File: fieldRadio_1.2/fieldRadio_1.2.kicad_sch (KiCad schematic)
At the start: 11 parts, among them J1 Conn_01x02, J12 AudioJack3_Switch, J18 Conn_01x16, J2 Conn_01x02, J3 Conn_01x03, J4 AudioJack2_Switch, J5 AudioJack3_Switch, J7 Conn_01x04, J8 Conn_01x12

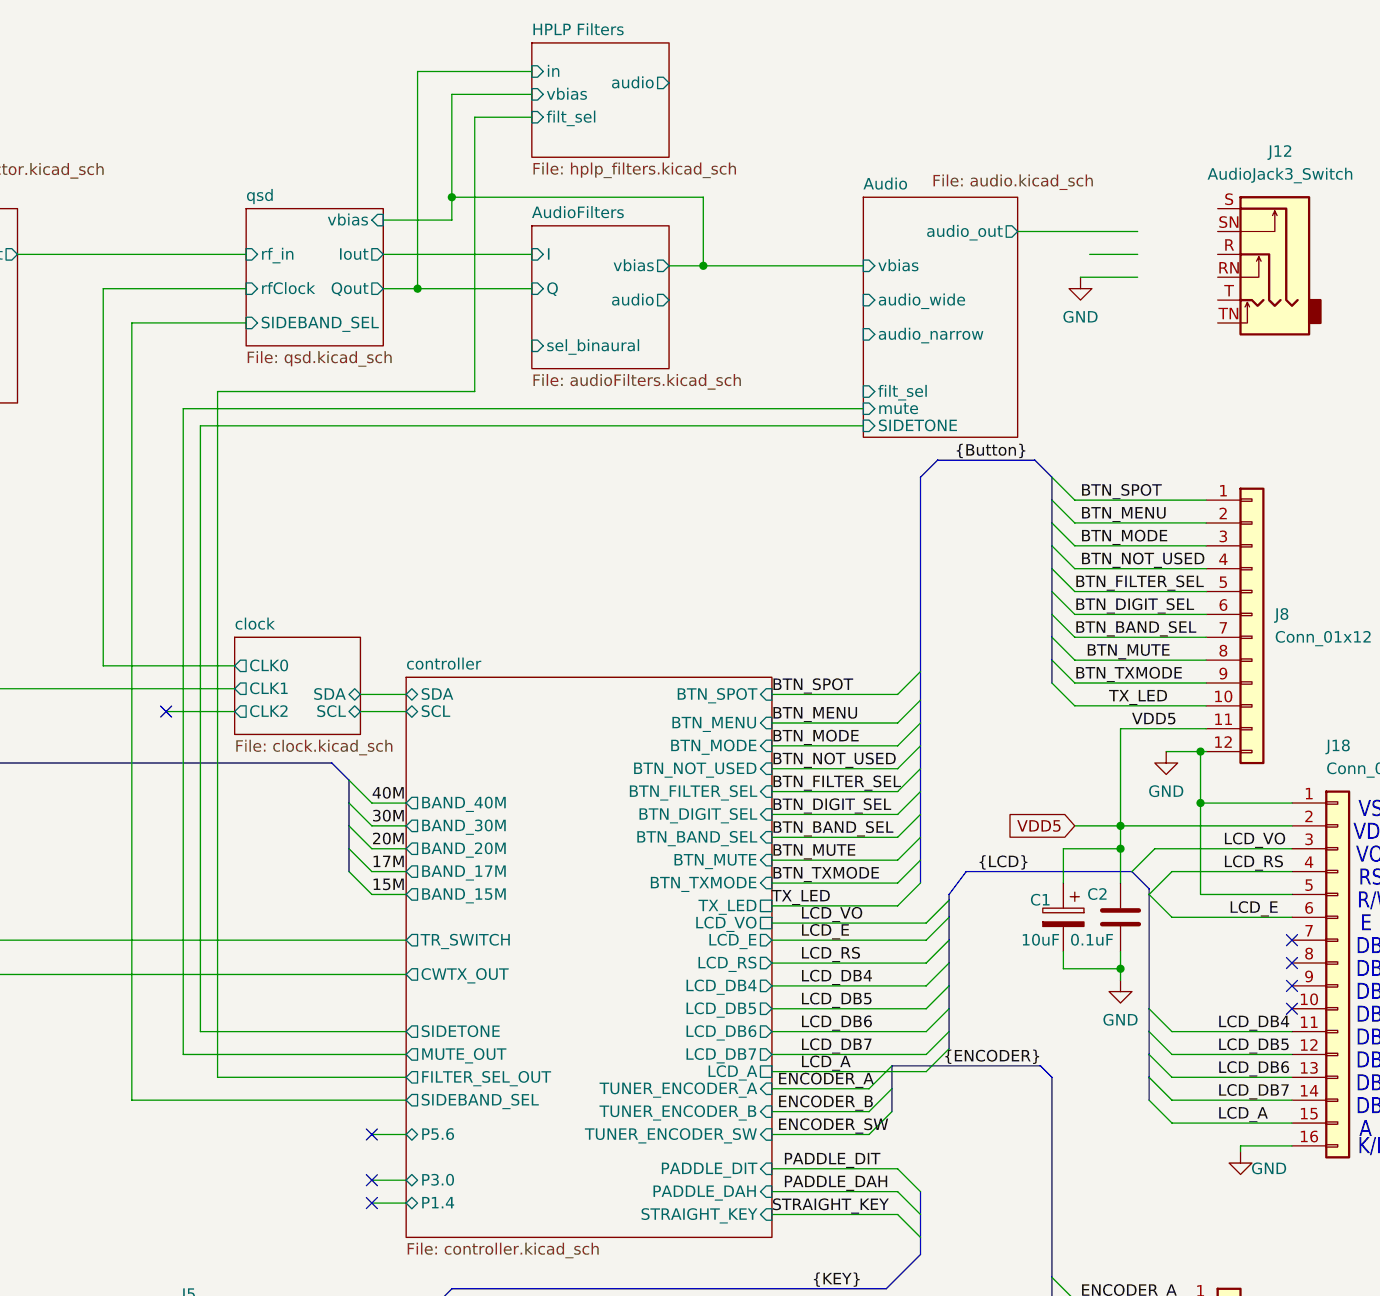
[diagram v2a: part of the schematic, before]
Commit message: Finished first pass of audio schematic changes for binaural/mono
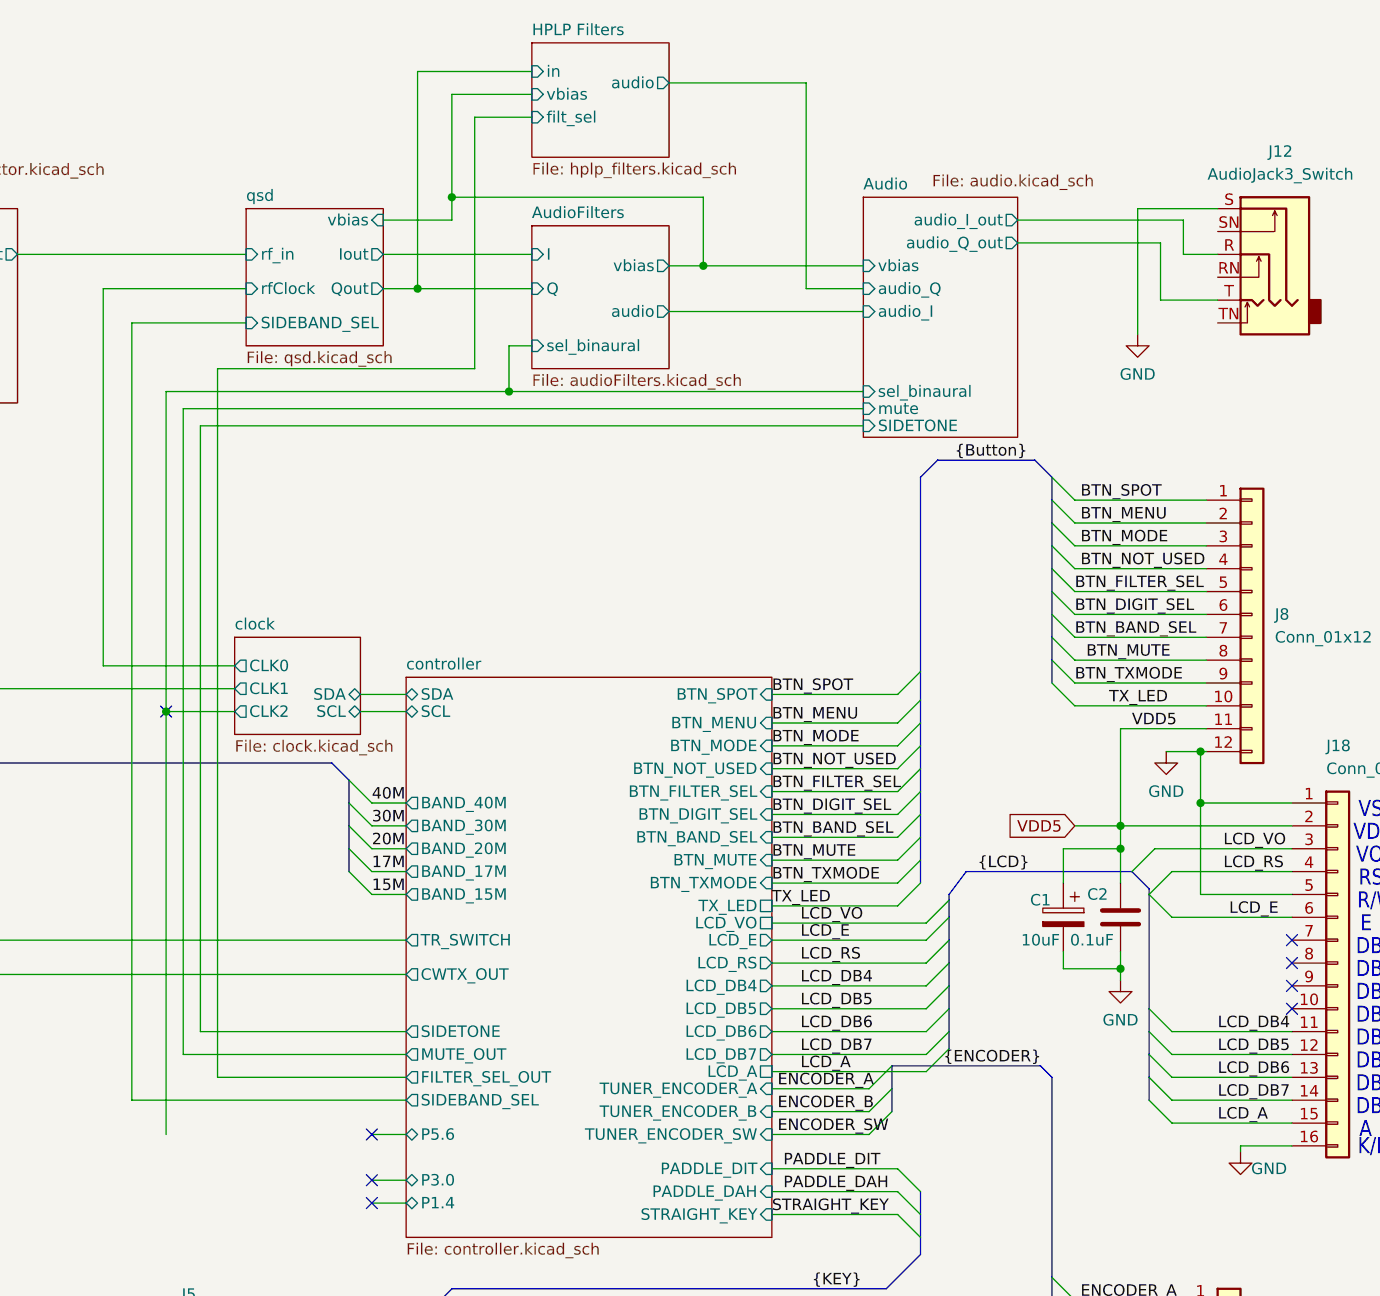
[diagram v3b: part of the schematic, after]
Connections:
- net GND: now also J12.S
- net Audio/audio_I_out: now reaches J12.R
- net Audio/audio_Q_out: now reaches J12.T
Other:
- sheet Audio ports: added audio_I, audio_I_out, audio_Q, audio_Q_out, sel_binaural; removed audio_narrow, audio_out, audio_wide, filt_sel
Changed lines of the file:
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@@
 	)
 	(junction
+		(at 144.78 90.17)
+		(diameter 0)
+		(color 0 0 0 0)
+	)
+	(junction
 		(at 204.47 40.64)
 		(diameter 0)
@@
 	)
 	(junction
+		(at 182.88 54.61)
+		(diameter 0)
+		(color 0 0 0 0)
+	)
+	(junction
 		(at 250.825 105.41)
 		(diameter 0)
@@
 		)
 	)
+	(wire
+		(pts
+			(xy 252.73 34.29) (xy 252.73 48.26)
+		)
+		(stroke
+			(width 0)
+			(type default)
+		)
+	)
 	(bus
 		(pts
@@
 	(wire
 		(pts
-			(xy 150.495 130.81) (xy 150.495 54.61)
+			(xy 150.495 130.81) (xy 150.495 52.07)
 		)
 		(stroke
@@
 	(wire
 		(pts
+			(xy 144.78 90.17) (xy 144.78 137.16)
+		)
+		(stroke
+			(width 0)
+			(type default)
+		)
+	)
+	(wire
+		(pts
 			(xy 171.45 130.81) (xy 150.495 130.81)
 		)
@@
 	(wire
 		(pts
+			(xy 182.88 49.53) (xy 182.88 54.61)
+		)
+		(stroke
+			(width 0)
+			(type default)
+		)
+	)
+	(wire
+		(pts
 			(xy 146.685 56.515) (xy 222.25 56.515)
 		)
@@
 	(wire
 		(pts
+			(xy 255.27 44.45) (xy 261.62 44.45)
+		)
+		(stroke
+			(width 0)
+			(type default)
+		)
+	)
+	(wire
+		(pts
 			(xy 250.825 102.87) (xy 269.875 102.87)
 		)
@@
 	(wire
 		(pts
+			(xy 257.81 35.56) (xy 257.81 39.37)
+		)
+		(stroke
+			(width 0)
+			(type default)
+		)
+	)
+	(wire
+		(pts
 			(xy 259.715 110.49) (xy 269.875 110.49)
 		)
@@
 	(wire
 		(pts
+			(xy 222.25 54.61) (xy 182.88 54.61)
+		)
+		(stroke
+			(width 0)
+			(type default)
+		)
+	)
+	(wire
+		(pts
+			(xy 239.395 35.56) (xy 257.81 35.56)
+		)
+		(stroke
+			(width 0)
+			(type default)
+		)
+	)
+	(wire
+		(pts
 			(xy 71.755 180.34) (xy 71.755 184.785)
 		)
@@
 	(wire
 		(pts
-			(xy 150.495 54.61) (xy 179.07 54.61)
+			(xy 150.495 52.07) (xy 179.07 52.07)
 		)
 		(stroke
@@
 	(wire
 		(pts
+			(xy 215.9 43.18) (xy 222.25 43.18)
+		)
+		(stroke
+			(width 0)
+			(type default)
+		)
+	)
+	(wire
+		(pts
 			(xy 212.09 134.62) (xy 222.885 134.62)
 		)
@@
 	(wire
 		(pts
-			(xy 252.73 39.37) (xy 247.396 39.37)
-		)
-		(stroke
-			(width 0)
-			(type default)
-		)
-	)
-	(wire
-		(pts
 			(xy 256.54 128.27) (xy 269.875 128.27)
 		)
@@
 		)
 	)
+	(wire
+		(pts
+			(xy 257.81 39.37) (xy 261.62 39.37)
+		)
+		(stroke
+			(width 0)
+			(type default)
+		)
+	)
 	(bus
 		(pts
@@
 		)
 	)
-	(wire
+	(bus
 		(pts
-			(xy 246.38 41.91) (xy 252.73 41.91)
+			(xy 228.6 148.59) (xy 228.6 150.495)
 		)
 		(stroke
@@
 	(bus
 		(pts
-			(xy 228.6 148.59) (xy 228.6 150.495)
+			(xy 165.1 97.79) (xy 165.1 100.33)
 		)
 		(stroke
@@
 		)
 	)
-	(bus
+	(wire
 		(pts
-			(xy 165.1 97.79) (xy 165.1 100.33)
+			(xy 144.78 54.61) (xy 144.78 90.17)
 		)
 		(stroke
@@
 		)
 	)
+	(wire
+		(pts
+			(xy 215.9 20.32) (xy 215.9 43.18)
+		)
+		(stroke
+			(width 0)
+			(type default)
+		)
+	)
 	(bus
 		(pts
@@
 	(wire
 		(pts
+			(xy 239.395 38.1) (xy 255.27 38.1)
+		)
+		(stroke
+			(width 0)
+			(type default)
+		)
+	)
+	(wire
+		(pts
 			(xy 31.496 175.26) (xy 41.91 175.26)
 		)
@@
 		)
 	)
+	(wire
+		(pts
+			(xy 255.27 38.1) (xy 255.27 44.45)
+		)
+		(stroke
+			(width 0)
+			(type default)
+		)
+	)
 	(bus
 		(pts
@@
 	(wire
 		(pts
-			(xy 179.07 24.13) (xy 179.07 54.61)
+			(xy 179.07 24.13) (xy 179.07 52.07)
 		)
 		(stroke
@@
 	(wire
 		(pts
+			(xy 182.88 54.61) (xy 144.78 54.61)
+		)
+		(stroke
+			(width 0)
+			(type default)
+		)
+	)
+	(wire
+		(pts
 			(xy 200.66 40.64) (xy 204.47 40.64)
 		)
@@
 		)
 	)
+	(wire
+		(pts
+			(xy 200.66 20.32) (xy 215.9 20.32)
+		)
+		(stroke
+			(width 0)
+			(type default)
+		)
+	)
 	(bus
 		(pts
@@
 		)
 	)
+	(wire
+		(pts
+			(xy 200.66 45.72) (xy 222.25 45.72)
+		)
+		(stroke
+			(width 0)
+			(type default)
+		)
+	)
 	(bus
 		(pts
@@
 	(wire
 		(pts
-			(xy 239.395 36.83) (xy 252.73 36.83)
-		)
-		(stroke
-			(width 0)
-			(type default)
-		)
-	)
-	(wire
-		(pts
 			(xy 167.64 137.16) (xy 171.45 137.16)
 		)
@@
 	(wire
 		(pts
+			(xy 185.42 49.53) (xy 182.88 49.53)
+		)
+		(stroke
+			(width 0)
+			(type default)
+		)
+	)
+	(wire
+		(pts
 			(xy 167.64 100.33) (xy 171.45 100.33)
 		)
@@
 	(wire
 		(pts
+			(xy 261.62 34.29) (xy 252.73 34.29)
+		)
+		(stroke
+			(width 0)
+			(type default)
+		)
+	)
+	(wire
+		(pts
 			(xy 56.515 43.18) (xy 64.77 43.18)
 		)
@@
 	(symbol
 		(lib_id "power:GND")
-		(at 246.38 41.91 0)
+		(at 252.73 48.26 0)
 		(unit 1)
 		(exclude_from_sim no)
@@
 		(fields_autoplaced yes)
 		(property "Reference" "#PWR04"
-			(at 246.38 48.26 0)
+			(at 252.73 54.61 0)
 			(effects
 				(font
@@
 		)
 		(property "Value" "GND"
-			(at 246.38 46.355 0)
+			(at 252.73 52.705 0)
 			(effects
 				(font
@@
 		)
 		(property "Footprint" ""
-			(at 246.38 41.91 0)
+			(at 252.73 48.26 0)
 			(effects
 				(font
@@
 		)
 		(property "Datasheet" ""
-			(at 246.38 41.91 0)
+			(at 252.73 48.26 0)
 			(effects
 				(font
@@
 		)
 		(property "Description" ""
-			(at 246.38 41.91 0)
+			(at 252.73 48.26 0)
 			(effects
 				(font
@@
 			)
 		)
-		(pin "audio_narrow" input
-			(at 222.25 48.26 180)
+		(pin "vbias" input
+			(at 222.25 40.64 180)
 			(effects
 				(font
@@
 			)
 		)
-		(pin "audio_wide" input
-			(at 222.25 44.45 180)
+		(pin "mute" input
+			(at 222.25 56.515 180)
 			(effects
 				(font
@@
 			)
 		)
-		(pin "vbias" input
-			(at 222.25 40.64 180)
+		(pin "SIDETONE" input
+			(at 222.25 58.42 180)
 			(effects
 				(font
@@
 			)
 		)
-		(pin "filt_sel" input
-			(at 222.25 54.61 180)
+		(pin "audio_Q_out" output
+			(at 239.395 38.1 0)
+			(effects
+				(font
+					(size 1.27 1.27)
+				)
+				(justify right)
+			)
+		)
+		(pin "audio_I" input
+			(at 222.25 45.72 180)
 			(effects
 				(font
@@
 			)
 		)
-		(pin "mute" input
-			(at 222.25 56.515 180)
+		(pin "audio_Q" input
+			(at 222.25 43.18 180)
 			(effects
 				(font
@@
 			)
 		)
-		(pin "SIDETONE" input
-			(at 222.25 58.42 180)
+		(pin "sel_binaural" input
+			(at 222.25 54.61 180)
 			(effects
 				(font
@@
 			)
 		)
-		(pin "audio_out" output
-			(at 239.395 36.83 0)
+		(pin "audio_I_out" output
+			(at 239.395 35.56 0)
 			(effects
 				(font
@@
 		)
 		(pin "audio" output
-			(at 200.66 44.45 0)
+			(at 200.66 45.72 0)
 			(effects
 				(font

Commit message: Added new power output amp changes from QEX
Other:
- sheet powerAmp ports: added VDD_AMP_enable, bst_enable, vdrv_enable, ~{rf_enable}; removed none
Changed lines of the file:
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@@
 	(wire
 		(pts
-			(xy 72.39 60.96) (xy 59.69 60.96)
+			(xy 67.945 60.96) (xy 59.69 60.96)
 		)
 		(stroke
@@
 	)
 	(sheet
-		(at 72.39 58.42)
-		(size 16.51 7.62)
+		(at 67.945 58.42)
+		(size 20.955 17.78)
 		(exclude_from_sim no)
 		(in_bom yes)
@@
 		)
 		(property "Sheetname" "powerAmp"
-			(at 72.39 57.7084 0)
+			(at 67.945 57.7084 0)
 			(effects
 				(font
@@
 		)
 		(property "Sheetfile" "powerAmp.kicad_sch"
-			(at 72.39 54.61 0)
+			(at 67.945 54.61 0)
 			(effects
 				(font
@@
 		)
 		(pin "pwrOut" output
-			(at 72.39 60.96 180)
+			(at 67.945 60.96 180)
 			(effects
 				(font
@@
 			)
 		)
+		(pin "bst_enable" input
+			(at 67.945 66.04 180)
+			(effects
+				(font
+					(size 1.27 1.27)
+				)
+				(justify left)
+			)
+		)
+		(pin "VDD_AMP_enable" input
+			(at 67.945 68.58 180)
+			(effects
+				(font
+					(size 1.27 1.27)
+				)
+				(justify left)
+			)
+		)
+		(pin "vdrv_enable" input
+			(at 67.945 71.12 180)
+			(effects
+				(font
+					(size 1.27 1.27)
+				)
+				(justify left)
+			)
+		)
+		(pin "~{rf_enable}" input
+			(at 67.945 73.66 180)
+			(effects
+				(font
+					(size 1.27 1.27)
+				)
+				(justify left)
+			)
+		)
